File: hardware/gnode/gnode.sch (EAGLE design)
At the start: 11 parts, among them IC1 HTU21D, U1 ATMEGA328P_TQFP

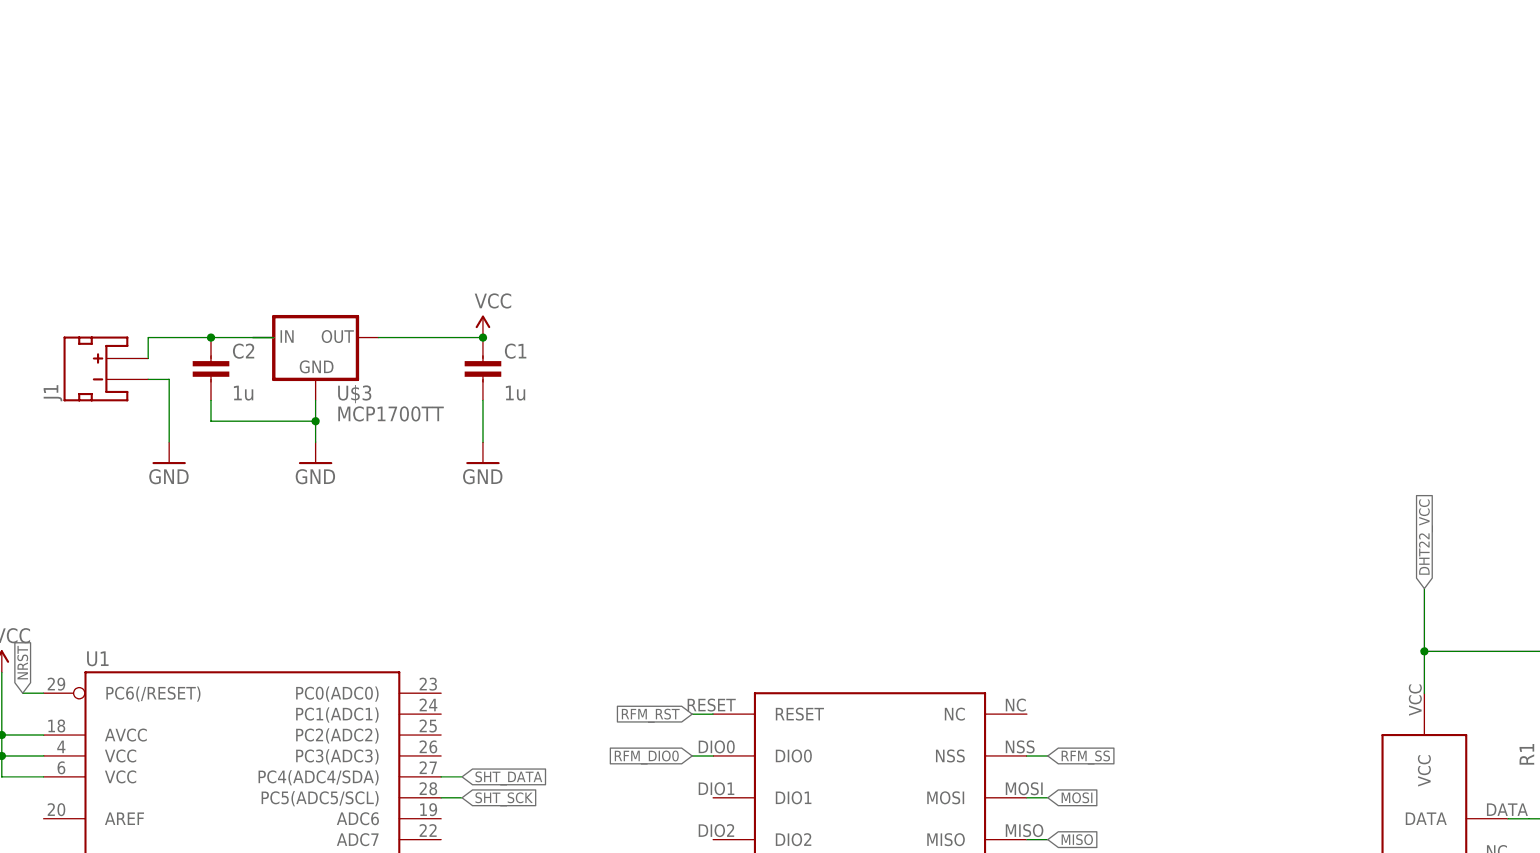
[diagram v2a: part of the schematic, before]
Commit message: added cn3083 solar charger
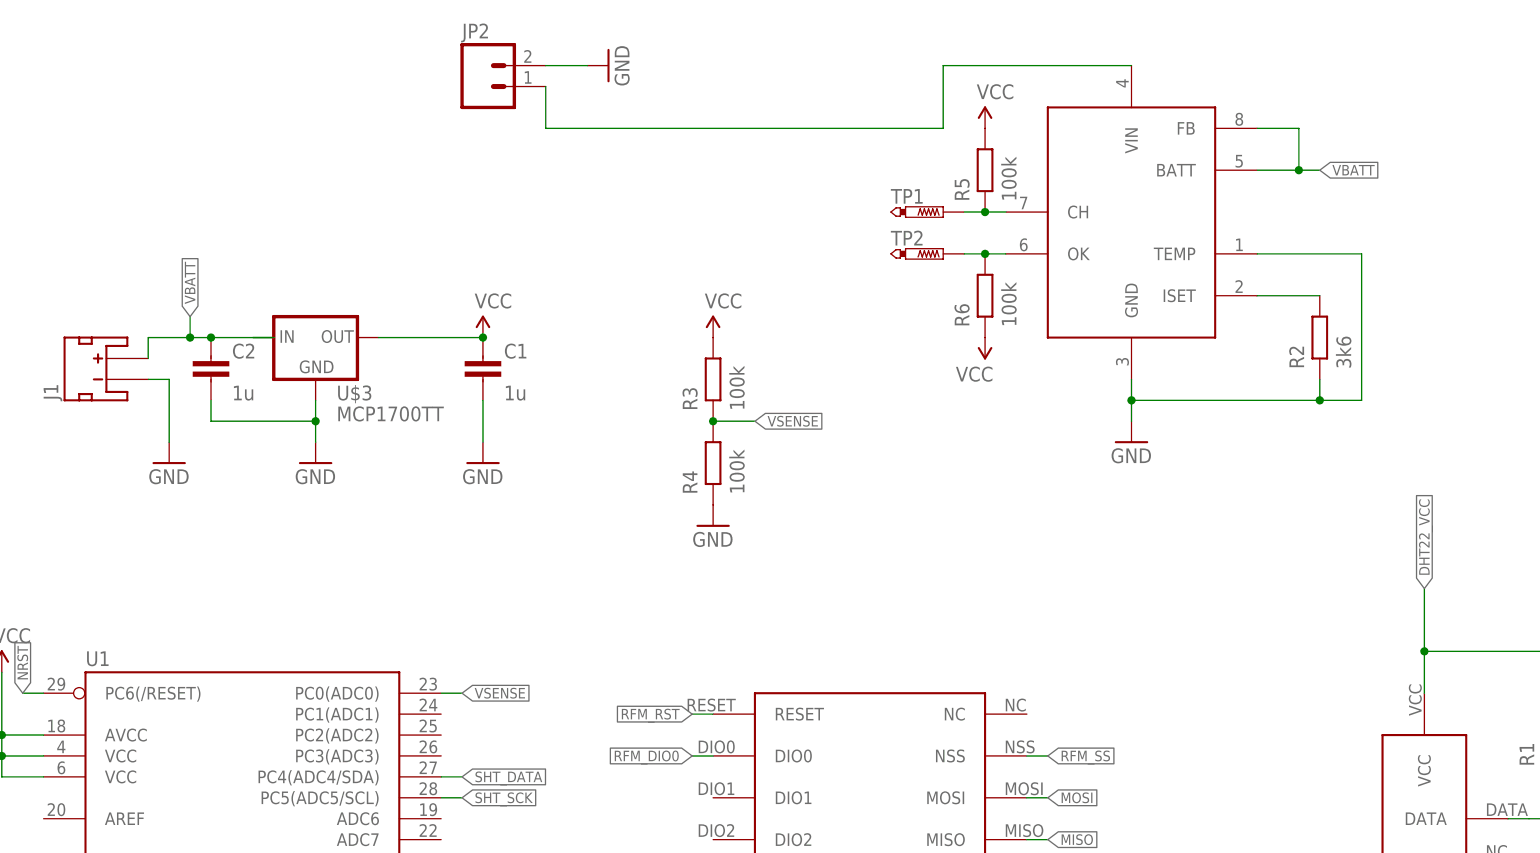
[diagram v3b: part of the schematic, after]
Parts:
- added JP2: (no value), Mine:M02PTH
- added R2: 3k6, passives-7351:RESISTOR0603-N
- added R3, R4, R5, R6: 100k, passives-7351:RESISTOR0603-N
- added TP1, TP2: PTR1B1,27, testpad:PTR1B1,27
- added U$4: CN3083, jonsowman:CN3083
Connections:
- new net N$3: JP2.1, U$4.VIN
- new net N$4: R2.P$2, U$4.ISET
- new net N$5: R6.P$2, TP2.TP, U$4.OK
- new net VBATT: C2.1, J1.+, U$3.IN, U$4.BATT, U$4.FB
- new net VSENSE: R3.P$1, R4.P$2, U1.PC0(ADC0)
- net GND: now also JP2.2, R2.P$1, R4.P$1, U$4.GND, U$4.TEMP
- net N$2: now also R5.P$1, TP1.TP, U$4.CH; no longer C2.1, J1.+, U$3.IN
- net VCC: now also R3.P$2, R5.P$2, R6.P$1
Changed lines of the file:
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@@
 <part name="U$3" library="dtb" deviceset="MCP1700" device="TT"/>
 <part name="C2" library="passives-7351" deviceset="CAPACITOR" device="0603-N" value="1u"/>
+<part name="U$4" library="jonsowman" deviceset="CN3083" device=""/>
+<part name="JP2" library="Mine" deviceset="M02" device="PTH"/>
+<part name="GND10" library="SparkFun-Aesthetics" deviceset="GND" device=""/>
+<part name="GND11" library="SparkFun-Aesthetics" deviceset="GND" device=""/>
+<part name="R2" library="passives-7351" deviceset="RESISTOR" device="0603-N" value="3k6"/>
+<part name="SUPPLY6" library="SparkFun-Aesthetics" deviceset="VCC" device=""/>
+<part name="GND12" library="SparkFun-Aesthetics" deviceset="GND" device=""/>
+<part name="R3" library="passives-7351" deviceset="RESISTOR" device="0603-N" value="100k"/>
+<part name="R4" library="passives-7351" deviceset="RESISTOR" device="0603-N" value="100k"/>
+<part name="TP1" library="testpad" deviceset="PTR1" device="B1,27"/>
+<part name="TP2" library="testpad" deviceset="PTR1" device="B1,27"/>
+<part name="R5" library="passives-7351" deviceset="RESISTOR" device="0603-N" value="100k"/>
+<part name="R6" library="passives-7351" deviceset="RESISTOR" device="0603-N" value="100k"/>
+<part name="SUPPLY7" library="SparkFun-Aesthetics" deviceset="VCC" device=""/>
+<part name="SUPPLY8" library="SparkFun-Aesthetics" deviceset="VCC" device=""/>
 </parts>
 <sheets>
@@
 <instance part="U$3" gate="G$1" x="-2.54" y="109.22"/>
 <instance part="C2" gate="G$1" x="-15.24" y="106.68"/>
+<instance part="U$4" gate="G$1" x="96.52" y="129.54"/>
+<instance part="JP2" gate="G$1" x="17.78" y="139.7"/>
+<instance part="GND10" gate="1" x="33.02" y="142.24" rot="R90"/>
+<instance part="GND11" gate="1" x="96.52" y="96.52"/>
+<instance part="R2" gate="G$1" x="119.38" y="109.22" rot="R90"/>
+<instance part="SUPPLY6" gate="G$1" x="45.72" y="109.22"/>
+<instance part="GND12" gate="1" x="45.72" y="86.36"/>
+<instance part="R3" gate="G$1" x="45.72" y="104.14" rot="R90"/>
+<instance part="R4" gate="G$1" x="45.72" y="93.98" rot="R90"/>
+<instance part="TP1" gate="G$1" x="73.66" y="124.46" rot="R270"/>
+<instance part="TP2" gate="G$1" x="73.66" y="119.38" rot="R270"/>
+<instance part="R5" gate="G$1" x="78.74" y="129.54" rot="R90"/>
+<instance part="R6" gate="G$1" x="78.74" y="114.3" rot="R90"/>
+<instance part="SUPPLY7" gate="G$1" x="78.74" y="134.62"/>
+<instance part="SUPPLY8" gate="G$1" x="78.74" y="109.22" rot="R180"/>
 </instances>
 <busses>
@@
 <junction x="-2.54" y="99.06"/>
 </segment>
+<segment>
+<pinref part="GND10" gate="1" pin="GND"/>
+<pinref part="JP2" gate="G$1" pin="2"/>
+<wire x1="30.48" y1="142.24" x2="25.4" y2="142.24" width="0.1524" layer="91"/>
+</segment>
+<segment>
+<pinref part="U$4" gate="G$1" pin="GND"/>
+<pinref part="GND11" gate="1" pin="GND"/>
+<wire x1="96.52" y1="104.14" x2="96.52" y2="101.6" width="0.1524" layer="91"/>
+<pinref part="R2" gate="G$1" pin="P$1"/>
+<wire x1="96.52" y1="101.6" x2="96.52" y2="99.06" width="0.1524" layer="91"/>
+<wire x1="119.38" y1="104.14" x2="119.38" y2="101.6" width="0.1524" layer="91"/>
+<wire x1="119.38" y1="101.6" x2="96.52" y2="101.6" width="0.1524" layer="91"/>
+<junction x="96.52" y="101.6"/>
+<pinref part="U$4" gate="G$1" pin="TEMP"/>
+<wire x1="111.76" y1="119.38" x2="124.46" y2="119.38" width="0.1524" layer="91"/>
+<wire x1="124.46" y1="119.38" x2="124.46" y2="101.6" width="0.1524" layer="91"/>
+<wire x1="124.46" y1="101.6" x2="119.38" y2="101.6" width="0.1524" layer="91"/>
+<junction x="119.38" y="101.6"/>
+</segment>
+<segment>
+<pinref part="GND12" gate="1" pin="GND"/>
+<pinref part="R4" gate="G$1" pin="P$1"/>
+</segment>
 </net>
 <net name="N$1" class="0">
@@
 <wire x1="33.02" y1="-12.7" x2="33.02" y2="-10.16" width="0.1524" layer="91"/>
 </segment>
-</net>
-<net name="N$2" class="0">
+<segment>
+<pinref part="SUPPLY6" gate="G$1" pin="VCC"/>
+<pinref part="R3" gate="G$1" pin="P$2"/>
+</segment>
+<segment>
+<pinref part="R5" gate="G$1" pin="P$2"/>
+<pinref part="SUPPLY7" gate="G$1" pin="VCC"/>
+</segment>
+<segment>
+<pinref part="R6" gate="G$1" pin="P$1"/>
+<pinref part="SUPPLY8" gate="G$1" pin="VCC"/>
+</segment>
+</net>
+<net name="VBATT" class="0">
 <segment>
 <pinref part="J1" gate="G$1" pin="+"/>
 <wire x1="-10.16" y1="109.22" x2="-7.62" y2="109.22" width="0.1524" layer="91"/>
 <wire x1="-7.62" y1="109.22" x2="-15.24" y2="109.22" width="0.1524" layer="91"/>
-<wire x1="-15.24" y1="109.22" x2="-22.86" y2="109.22" width="0.1524" layer="91"/>
+<wire x1="-15.24" y1="109.22" x2="-17.78" y2="109.22" width="0.1524" layer="91"/>
+<wire x1="-17.78" y1="109.22" x2="-22.86" y2="109.22" width="0.1524" layer="91"/>
 <wire x1="-22.86" y1="109.22" x2="-22.86" y2="106.68" width="0.1524" layer="91"/>
 <pinref part="U$3" gate="G$1" pin="IN"/>
 <pinref part="C2" gate="G$1" pin="1"/>
 <junction x="-15.24" y="109.22"/>
+<wire x1="-17.78" y1="109.22" x2="-17.78" y2="111.76" width="0.1524" layer="91"/>
+<junction x="-17.78" y="109.22"/>
+<label x="-17.78" y="111.76" size="1.27" layer="95" rot="R90" xref="yes"/>
+</segment>
+<segment>
+<pinref part="U$4" gate="G$1" pin="BATT"/>
+<wire x1="111.76" y1="129.54" x2="116.84" y2="129.54" width="0.1524" layer="91"/>
+<label x="119.38" y="129.54" size="1.27" layer="95" xref="yes"/>
+<pinref part="U$4" gate="G$1" pin="FB"/>
+<wire x1="116.84" y1="129.54" x2="119.38" y2="129.54" width="0.1524" layer="91"/>
+<wire x1="111.76" y1="134.62" x2="116.84" y2="134.62" width="0.1524" layer="91"/>
+<wire x1="116.84" y1="134.62" x2="116.84" y2="129.54" width="0.1524" layer="91"/>
+<junction x="116.84" y="129.54"/>
 </segment>
 </net>
@@
 </segment>
 </net>
+<net name="N$3" class="0">
+<segment>
+<pinref part="JP2" gate="G$1" pin="1"/>
+<wire x1="25.4" y1="139.7" x2="25.4" y2="134.62" width="0.1524" layer="91"/>
+<wire x1="25.4" y1="134.62" x2="73.66" y2="134.62" width="0.1524" layer="91"/>
+<wire x1="73.66" y1="134.62" x2="73.66" y2="142.24" width="0.1524" layer="91"/>
+<pinref part="U$4" gate="G$1" pin="VIN"/>
+<wire x1="73.66" y1="142.24" x2="96.52" y2="142.24" width="0.1524" layer="91"/>
+</segment>
+</net>
+<net name="N$4" class="0">
+<segment>
+<pinref part="U$4" gate="G$1" pin="ISET"/>
+<pinref part="R2" gate="G$1" pin="P$2"/>
+<wire x1="111.76" y1="114.3" x2="119.38" y2="114.3" width="0.1524" layer="91"/>
+</segment>
+</net>
+<net name="VSENSE" class="0">
+<segment>
+<pinref part="U1" gate="U$1" pin="PC0(ADC0)"/>
+<wire x1="12.7" y1="66.04" x2="15.24" y2="66.04" width="0.1524" layer="91"/>
+<label x="15.24" y="66.04" size="1.27" layer="95" xref="yes"/>
+</segment>
+<segment>
+<pinref part="R3" gate="G$1" pin="P$1"/>
+<pinref part="R4" gate="G$1" pin="P$2"/>
+<wire x1="45.72" y1="99.06" x2="50.8" y2="99.06" width="0.1524" layer="91"/>
+<junction x="45.72" y="99.06"/>
+<label x="50.8" y="99.06" size="1.27" layer="95" xref="yes"/>
+</segment>
+</net>
+<net name="N$2" class="0">
+<segment>
+<pinref part="U$4" gate="G$1" pin="CH"/>
+<pinref part="TP1" gate="G$1" pin="TP"/>
+<wire x1="76.2" y1="124.46" x2="78.74" y2="124.46" width="0.1524" layer="91"/>
+<pinref part="R5" gate="G$1" pin="P$1"/>
+<wire x1="78.74" y1="124.46" x2="81.28" y2="124.46" width="0.1524" layer="91"/>
+<junction x="78.74" y="124.46"/>
+</segment>
+</net>
+<net name="N$5" class="0">
+<segment>
+<pinref part="U$4" gate="G$1" pin="OK"/>
+<pinref part="TP2" gate="G$1" pin="TP"/>
+<wire x1="76.2" y1="119.38" x2="78.74" y2="119.38" width="0.1524" layer="91"/>
+<pinref part="R6" gate="G$1" pin="P$2"/>
+<wire x1="78.74" y1="119.38" x2="81.28" y2="119.38" width="0.1524" layer="91"/>
+<junction x="78.74" y="119.38"/>
+</segment>
+</net>
